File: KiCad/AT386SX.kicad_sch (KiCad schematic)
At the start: 35 parts, among them J13 Front Panel, J14 CPU 1-25, J15 CPU 26-50, J16 CPU 51-75, J17 CPU 76-100, Q1 2N3904, SW1 Power, SW2 Reset, U1 80386SX, U2 80387SX, U3 RC2016A5, U7 74HC05, X1 CPU_CLK, X2 FPU_CLK, Y1 14.31818MHz

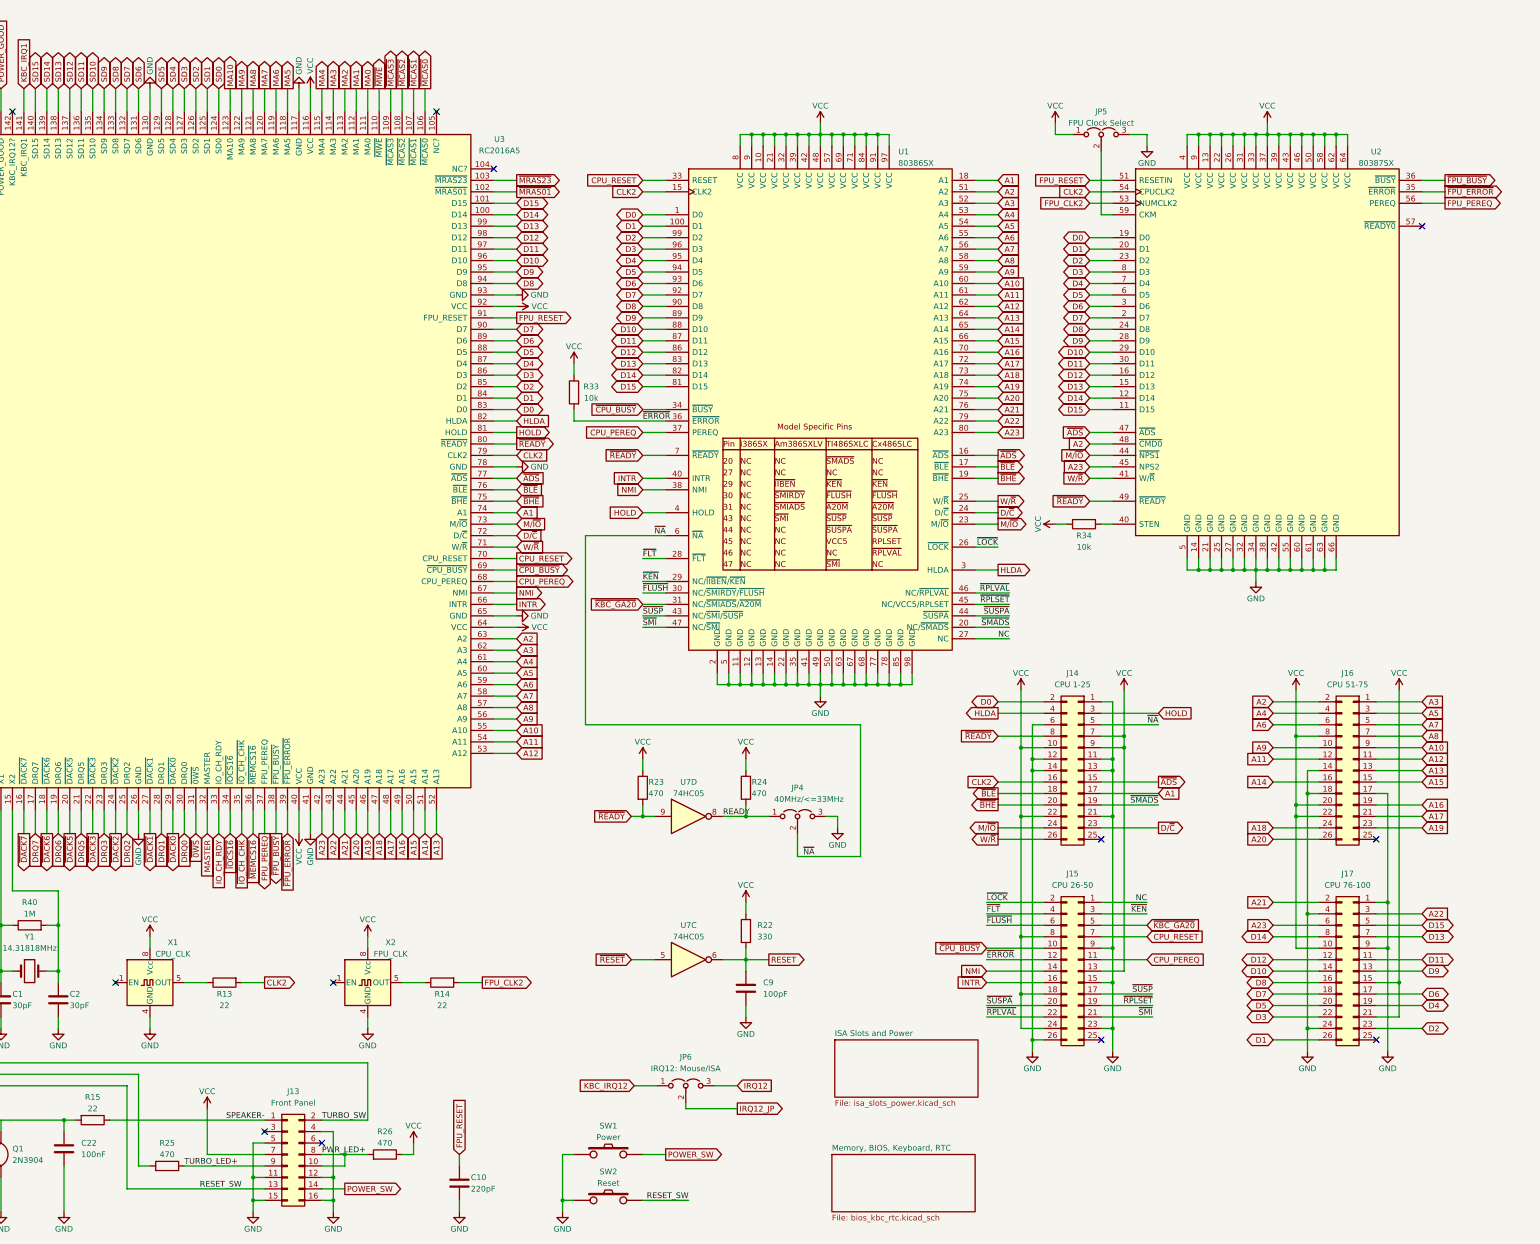
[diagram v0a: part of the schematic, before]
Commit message: Add a polyfuse for the PS/2 port
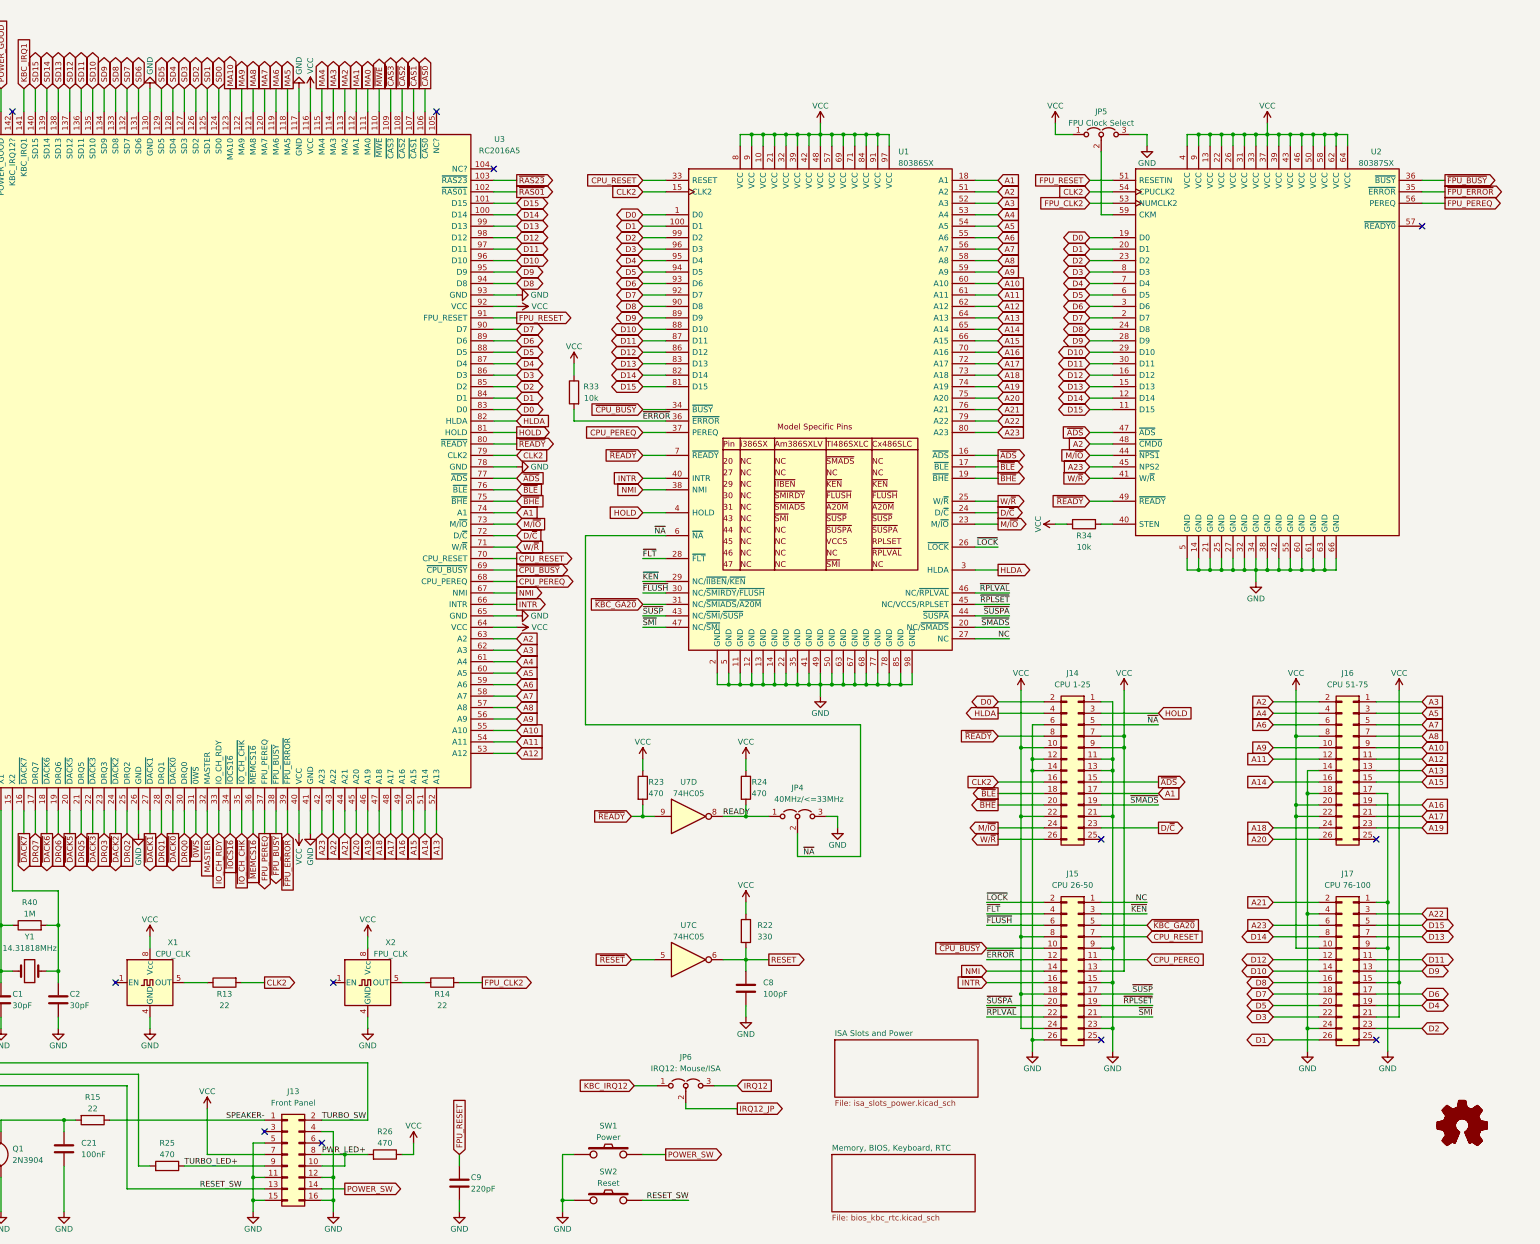
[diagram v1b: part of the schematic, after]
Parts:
- added LOGO1: Logo_Open_Hardware_Small, Symbol:OSHW-Logo2_7.3x6mm_SilkScreen, symbol Graphic:Logo_Open_Hardware_Small
- added LOGO2: Logo_Open_Hardware_Small, Symbol:KiCad-Logo2_5mm_SilkScreen, symbol Graphic:Logo_Open_Hardware_Small
- renumbered C22 to C21, C9 to C8, C10 to C9
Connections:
- net ~{MCAS0} renamed ~{CAS0}
- net ~{MCAS1} renamed ~{CAS1}
- net ~{MCAS2} renamed ~{CAS2}
- net ~{MCAS3} renamed ~{CAS3}
- net ~{MRAS01} renamed ~{RAS01}
- net ~{MRAS23} renamed ~{RAS23}

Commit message: Add version 2.3 files
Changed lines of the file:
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@@
   (title_block
     (title "386SX Motherboard Based on SARC RC2016 Chipset")
-    (date "2026-02-18")
-    (rev "2.2")
+    (date "2026-02-26")
+    (rev "2.3")
     (company "Copyright (C) 2024-2026 Sergey Kiselev")
     (comment 1 "https://github.com/Marco-Both/M396F-Replika")
@@
       (reference "#PWR0156") (unit 1) (value "VCC") (footprint "")
     )
+    (path "/1c0f074e-275c-4c09-93e3-0959df27fb02/32b90dd8-69d2-4559-8507-e6a06a379530"
+      (reference "#PWR0157") (unit 1) (value "GND") (footprint "")
+    )
     (path "/b64989fe-6b27-4acc-92bb-7beb2d401842"
